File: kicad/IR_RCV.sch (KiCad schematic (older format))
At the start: 6 parts, among them U7 AD8604

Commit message: 新基板，部品を配置
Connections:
- net +1.65VA: now also U7.12 (+); no longer U7.3 (+)
- net IR_RCV: now also U7.14; no longer U7.1
- net at C21.2, C22.1, R8.2: now also U7.13 (-); no longer U7.2 (-)
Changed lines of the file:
@@
 AR Path="/57CF292E/57CF0F37" Ref="D6"  Part="1"
 AR Path="/57CF2A30/57CF0F37" Ref="D7"  Part="1"
-F 0 "D4" H 4600 3950 50  0000 C CNN
+F 0 "D7" H 4600 3950 50  0000 C CNN
 F 1 "SFH213FA" H 4600 3750 50  0000 C CNN
 F 2 "mouse:Photo-5MM_Angle" H 4600 3850 50  0001 C CNN
@@
 $Comp
 L LM2902N U7
-U 1 1 57CF0F3E
+U 4 1 57CF0F3E
 P 5500 4000
 AR Path="/57CF0B09/57CF0F3E" Ref="U7"  Part="1"
@@
 F 2 "Housings_SSOP:TSSOP-14_4.4x5mm_Pitch0.65mm" H 5450 4100 50  0001 C CNN
 F 3 "" H 5550 4200 50  0000 C CNN
-	1    5500 4000
+	4    5500 4000
 	1    0    0    -1
 $EndComp
@@
 AR Path="/57CF292E/57CF0F45" Ref="C26"  Part="1"
 AR Path="/57CF2A30/57CF0F45" Ref="C28"  Part="1"
-F 0 "C22" H 4875 4200 50  0000 L CNN
+F 0 "C28" H 4875 4200 50  0000 L CNN
 F 1 "0.01u" H 4875 4000 50  0000 L CNN
 F 2 "Capacitors_SMD:C_0402" H 4888 3950 50  0001 C CNN
@@
 AR Path="/57CF292E/57CF0F4C" Ref="R13"  Part="1"
 AR Path="/57CF2A30/57CF0F4C" Ref="R15"  Part="1"
-F 0 "R9" V 4680 4650 50  0000 C CNN
+F 0 "R15" V 4680 4650 50  0000 C CNN
 F 1 "100k" V 4600 4650 50  0000 C CNN
 F 2 "Resistors_SMD:R_0402" V 4530 4650 50  0001 C CNN
@@
 AR Path="/57CF292E/57CF0F57" Ref="R12"  Part="1"
 AR Path="/57CF2A30/57CF0F57" Ref="R14"  Part="1"
-F 0 "R8" V 5730 3600 50  0000 C CNN
+F 0 "R14" V 5730 3600 50  0000 C CNN
 F 1 "220k" V 5650 3600 50  0000 C CNN
 F 2 "Resistors_SMD:R_0402" V 5580 3600 50  0001 C CNN
@@
 AR Path="/57CF292E/57CF0F5E" Ref="C25"  Part="1"
 AR Path="/57CF2A30/57CF0F5E" Ref="C27"  Part="1"
-F 0 "C21" H 5550 3500 50  0000 L CNN
+F 0 "C27" H 5550 3500 50  0000 L CNN
 F 1 "22p" H 5500 3300 50  0000 L CNN
 F 2 "Capacitors_SMD:C_0402" H 5688 3250 50  0001 C CNN

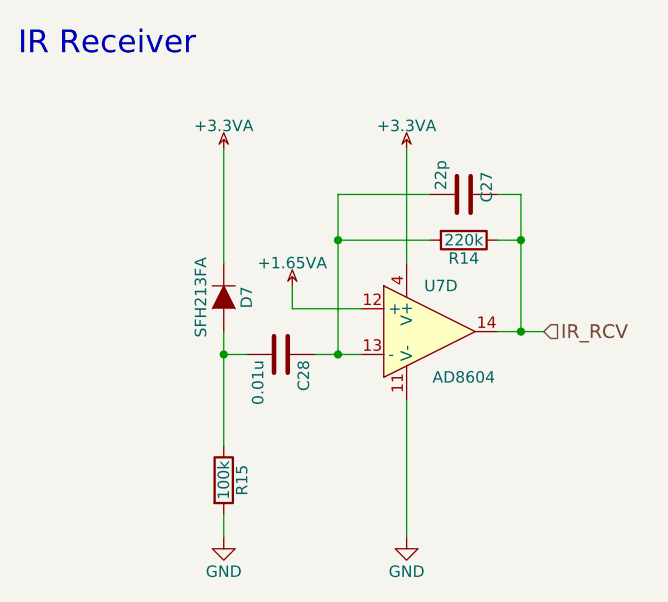
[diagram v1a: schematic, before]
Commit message: 自動配線用にdsn吐き出し
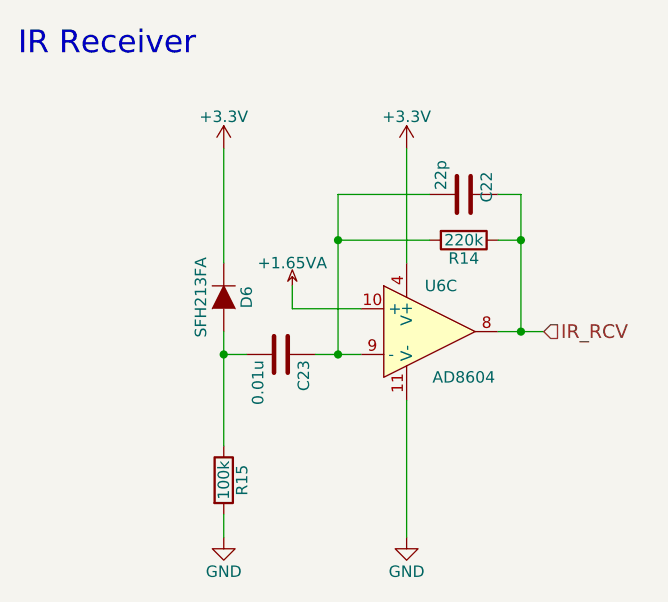
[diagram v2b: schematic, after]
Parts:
- renumbered C21 to C18, C22 to C19, R8 to R10, R9 to R11, U7 to U6
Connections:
- net +1.65VA: now also U6.10 (+); no longer U6.12 (+)
- net IR_RCV: now also U6.8; no longer U6.14
- net at C18.2, C19.1, R10.2: now also U6.9 (-); no longer U6.13 (-)
- net +3.3VADC renamed +3V3
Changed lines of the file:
@@
 $Descr A4 11693 8268
 encoding utf-8
-Sheet 6 15
+Sheet 8 15
 Title ""
 Date ""
@@
 AR Path="/57CF292E/57CF0F37" Ref="D6"  Part="1"
 AR Path="/57CF2A30/57CF0F37" Ref="D7"  Part="1"
-F 0 "D7" H 4600 3950 50  0000 C CNN
+F 0 "D6" H 4600 3950 50  0000 C CNN
 F 1 "SFH213FA" H 4600 3750 50  0000 C CNN
 F 2 "mouse:Photo-5MM_Angle" H 4600 3850 50  0001 C CNN
@@
 $EndComp
 $Comp
-L LM2902N U7
-U 4 1 57CF0F3E
+L LM2902N U6
+U 3 1 57CF0F3E
 P 5500 4000
-AR Path="/57CF0B09/57CF0F3E" Ref="U7"  Part="1"
-AR Path="/57CF289D/57CF0F3E" Ref="U7"  Part="2"
-AR Path="/57CF292E/57CF0F3E" Ref="U7"  Part="3"
-AR Path="/57CF2A30/57CF0F3E" Ref="U7"  Part="4"
-F 0 "U7" H 5550 4200 50  0000 C CNN
+AR Path="/57CF0B09/57CF0F3E" Ref="U6"  Part="1"
+AR Path="/57CF289D/57CF0F3E" Ref="U6"  Part="2"
+AR Path="/57CF292E/57CF0F3E" Ref="U6"  Part="3"
+AR Path="/57CF2A30/57CF0F3E" Ref="U6"  Part="4"
+F 0 "U6" H 5550 4200 50  0000 C CNN
 F 1 "AD8604" H 5650 3800 50  0000 C CNN
 F 2 "Housings_SSOP:TSSOP-14_4.4x5mm_Pitch0.65mm" H 5450 4100 50  0001 C CNN
 F 3 "" H 5550 4200 50  0000 C CNN
-	4    5500 4000
-	1    0    0    -1
-$EndComp
-$Comp
-L C C22
+	3    5500 4000
+	1    0    0    -1
+$EndComp
+$Comp
+L C C19
 U 1 1 57CF0F45
 P 4850 4100
-AR Path="/57CF0B09/57CF0F45" Ref="C22"  Part="1"
-AR Path="/57CF289D/57CF0F45" Ref="C24"  Part="1"
-AR Path="/57CF292E/57CF0F45" Ref="C26"  Part="1"
-AR Path="/57CF2A30/57CF0F45" Ref="C28"  Part="1"
-F 0 "C28" H 4875 4200 50  0000 L CNN
+AR Path="/57CF0B09/57CF0F45" Ref="C19"  Part="1"
+AR Path="/57CF289D/57CF0F45" Ref="C21"  Part="1"
+AR Path="/57CF292E/57CF0F45" Ref="C23"  Part="1"
+AR Path="/57CF2A30/57CF0F45" Ref="C25"  Part="1"
+F 0 "C23" H 4875 4200 50  0000 L CNN
 F 1 "0.01u" H 4875 4000 50  0000 L CNN
 F 2 "Capacitors_SMD:C_0402" H 4888 3950 50  0001 C CNN
@@
 $EndComp
 $Comp
-L R R9
+L R R11
 U 1 1 57CF0F4C
 P 4600 4650
-AR Path="/57CF0B09/57CF0F4C" Ref="R9"  Part="1"
-AR Path="/57CF289D/57CF0F4C" Ref="R11"  Part="1"
-AR Path="/57CF292E/57CF0F4C" Ref="R13"  Part="1"
-AR Path="/57CF2A30/57CF0F4C" Ref="R15"  Part="1"
+AR Path="/57CF0B09/57CF0F4C" Ref="R11"  Part="1"
+AR Path="/57CF289D/57CF0F4C" Ref="R13"  Part="1"
+AR Path="/57CF292E/57CF0F4C" Ref="R15"  Part="1"
+AR Path="/57CF2A30/57CF0F4C" Ref="R17"  Part="1"
 F 0 "R15" V 4680 4650 50  0000 C CNN
 F 1 "100k" V 4600 4650 50  0000 C CNN
@@
 Connection ~ 4600 4100
 $Comp
-L R R8
+L R R10
 U 1 1 57CF0F57
 P 5650 3600
-AR Path="/57CF0B09/57CF0F57" Ref="R8"  Part="1"
-AR Path="/57CF289D/57CF0F57" Ref="R10"  Part="1"
-AR Path="/57CF292E/57CF0F57" Ref="R12"  Part="1"
-AR Path="/57CF2A30/57CF0F57" Ref="R14"  Part="1"
+AR Path="/57CF0B09/57CF0F57" Ref="R10"  Part="1"
+AR Path="/57CF289D/57CF0F57" Ref="R12"  Part="1"
+AR Path="/57CF292E/57CF0F57" Ref="R14"  Part="1"
+AR Path="/57CF2A30/57CF0F57" Ref="R16"  Part="1"
 F 0 "R14" V 5730 3600 50  0000 C CNN
 F 1 "220k" V 5650 3600 50  0000 C CNN
@@
 $EndComp
 $Comp
-L C C21
+L C C18
 U 1 1 57CF0F5E
 P 5650 3400
-AR Path="/57CF0B09/57CF0F5E" Ref="C21"  Part="1"
-AR Path="/57CF289D/57CF0F5E" Ref="C23"  Part="1"
-AR Path="/57CF292E/57CF0F5E" Ref="C25"  Part="1"
-AR Path="/57CF2A30/57CF0F5E" Ref="C27"  Part="1"
-F 0 "C27" H 5550 3500 50  0000 L CNN
+AR Path="/57CF0B09/57CF0F5E" Ref="C18"  Part="1"
+AR Path="/57CF289D/57CF0F5E" Ref="C20"  Part="1"
+AR Path="/57CF292E/57CF0F5E" Ref="C22"  Part="1"
+AR Path="/57CF2A30/57CF0F5E" Ref="C24"  Part="1"
+F 0 "C22" H 5550 3500 50  0000 L CNN
 F 1 "22p" H 5500 3300 50  0000 L CNN
 F 2 "Capacitors_SMD:C_0402" H 5688 3250 50  0001 C CNN
@@
 Wire Wire Line
 	4600 3200 4600 3700
-$Comp
-L +3.3VA #PWR062
-U 1 1 57CF0F71
-P 4600 3200
-AR Path="/57CF0B09/57CF0F71" Ref="#PWR062"  Part="1"
-AR Path="/57CF289D/57CF0F71" Ref="#PWR067"  Part="1"
-AR Path="/57CF292E/57CF0F71" Ref="#PWR072"  Part="1"
-AR Path="/57CF2A30/57CF0F71" Ref="#PWR077"  Part="1"
-F 0 "#PWR077" H 4750 3150 50  0001 C CNN
-F 1 "+3.3VA" H 4600 3300 50  0000 C CNN
-F 2 "" H 4600 3200 50  0000 C CNN
-F 3 "" H 4600 3200 50  0000 C CNN
-	1    4600 3200
-	1    0    0    -1
-$EndComp
-$Comp
-L +3.3VA #PWR063
-U 1 1 57CF0F77
-P 5400 3200
-AR Path="/57CF0B09/57CF0F77" Ref="#PWR063"  Part="1"
-AR Path="/57CF289D/57CF0F77" Ref="#PWR068"  Part="1"
-AR Path="/57CF292E/57CF0F77" Ref="#PWR073"  Part="1"
-AR Path="/57CF2A30/57CF0F77" Ref="#PWR078"  Part="1"
-F 0 "#PWR078" H 5550 3150 50  0001 C CNN
-F 1 "+3.3VA" H 5400 3300 50  0000 C CNN
-F 2 "" H 5400 3200 50  0000 C CNN
-F 3 "" H 5400 3200 50  0000 C CNN
-	1    5400 3200
-	1    0    0    -1
-$EndComp
-$Comp
-L +1.65VA #PWR064
-U 1 1 57CF0F7D
-P 4900 3800
-AR Path="/57CF0B09/57CF0F7D" Ref="#PWR064"  Part="1"
-AR Path="/57CF289D/57CF0F7D" Ref="#PWR069"  Part="1"
-AR Path="/57CF292E/57CF0F7D" Ref="#PWR074"  Part="1"
-AR Path="/57CF2A30/57CF0F7D" Ref="#PWR079"  Part="1"
-F 0 "#PWR079" H 5050 3750 50  0001 C CNN
-F 1 "+1.65VA" H 4900 3900 50  0000 C CNN
-F 2 "" H 4900 3800 50  0000 C CNN
-F 3 "" H 4900 3800 50  0000 C CNN
-	1    4900 3800
-	1    0    0    -1
-$EndComp
 Wire Wire Line
 	4900 3800 4900 3900
@@
 	4900 3900 5200 3900
 $Comp
-L GND #PWR065
+L GND #PWR058
 U 1 1 57CF0F85
 P 4600 4900
-AR Path="/57CF0B09/57CF0F85" Ref="#PWR065"  Part="1"
-AR Path="/57CF289D/57CF0F85" Ref="#PWR070"  Part="1"
-AR Path="/57CF292E/57CF0F85" Ref="#PWR075"  Part="1"
-AR Path="/57CF2A30/57CF0F85" Ref="#PWR080"  Part="1"
-F 0 "#PWR080" H 4600 4650 50  0001 C CNN
+AR Path="/57CF0B09/57CF0F85" Ref="#PWR058"  Part="1"
+AR Path="/57CF289D/57CF0F85" Ref="#PWR063"  Part="1"
+AR Path="/57CF292E/57CF0F85" Ref="#PWR068"  Part="1"
+AR Path="/57CF2A30/57CF0F85" Ref="#PWR073"  Part="1"
+F 0 "#PWR073" H 4600 4650 50  0001 C CNN
 F 1 "GND" H 4600 4750 50  0000 C CNN
 F 2 "" H 4600 4900 50  0000 C CNN
@@
 	4600 4900 4600 4800
 $Comp
-L GND #PWR066
+L GND #PWR059
 U 1 1 57CF0F8C
 P 5400 4900
-AR Path="/57CF0B09/57CF0F8C" Ref="#PWR066"  Part="1"
-AR Path="/57CF289D/57CF0F8C" Ref="#PWR071"  Part="1"
-AR Path="/57CF292E/57CF0F8C" Ref="#PWR076"  Part="1"
-AR Path="/57CF2A30/57CF0F8C" Ref="#PWR081"  Part="1"
-F 0 "#PWR081" H 5400 4650 50  0001 C CNN
+AR Path="/57CF0B09/57CF0F8C" Ref="#PWR059"  Part="1"
+AR Path="/57CF289D/57CF0F8C" Ref="#PWR064"  Part="1"
+AR Path="/57CF292E/57CF0F8C" Ref="#PWR069"  Part="1"
+AR Path="/57CF2A30/57CF0F8C" Ref="#PWR074"  Part="1"
+F 0 "#PWR074" H 5400 4650 50  0001 C CNN
 F 1 "GND" H 5400 4750 50  0000 C CNN
 F 2 "" H 5400 4900 50  0000 C CNN
@@
 Text Notes 3700 2800 0    100  ~ 0
 IR Receiver
+$Comp
+L +1.65VA #PWR060
+U 1 1 57CF0F7D
+P 4900 3800
+AR Path="/57CF0B09/57CF0F7D" Ref="#PWR060"  Part="1"
+AR Path="/57CF289D/57CF0F7D" Ref="#PWR065"  Part="1"
+AR Path="/57CF292E/57CF0F7D" Ref="#PWR070"  Part="1"
+AR Path="/57CF2A30/57CF0F7D" Ref="#PWR075"  Part="1"
+F 0 "#PWR075" H 5050 3750 50  0001 C CNN
+F 1 "+1.65VA" H 4900 3900 50  0000 C CNN
+F 2 "" H 4900 3800 50  0000 C CNN
+F 3 "" H 4900 3800 50  0000 C CNN
+	1    4900 3800
+	1    0    0    -1
+$EndComp
+$Comp
+L +3.3V #PWR061
+U 1 1 586FEA9B
+P 4600 3200
+AR Path="/57CF0B09/586FEA9B" Ref="#PWR061"  Part="1"
+AR Path="/57CF292E/586FEA9B" Ref="#PWR071"  Part="1"
+AR Path="/57CF289D/586FEA9B" Ref="#PWR066"  Part="1"
+AR Path="/57CF2A30/586FEA9B" Ref="#PWR076"  Part="1"
+F 0 "#PWR076" H 4600 3050 50  0001 C CNN
+F 1 "+3.3V" H 4600 3340 50  0000 C CNN
+F 2 "" H 4600 3200 50  0000 C CNN
+F 3 "" H 4600 3200 50  0000 C CNN
+	1    4600 3200
+	1    0    0    -1
+$EndComp
+$Comp
+L +3.3V #PWR072
+U 1 1 586FEABF
+P 5400 3200
+AR Path="/57CF292E/586FEABF" Ref="#PWR072"  Part="1"
+AR Path="/57CF0B09/586FEABF" Ref="#PWR062"  Part="1"
+AR Path="/57CF289D/586FEABF" Ref="#PWR067"  Part="1"
+AR Path="/57CF2A30/586FEABF" Ref="#PWR077"  Part="1"
+F 0 "#PWR077" H 5400 3050 50  0001 C CNN
+F 1 "+3.3V" H 5400 3340 50  0000 C CNN
+F 2 "" H 5400 3200 50  0000 C CNN
+F 3 "" H 5400 3200 50  0000 C CNN
+	1    5400 3200
+	1    0    0    -1
+$EndComp
 $EndSCHEMATC
